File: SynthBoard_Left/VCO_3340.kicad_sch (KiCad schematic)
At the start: 49 parts, among them IC4 AS321KTR-G1, IC5 V3340M, SW1 MFP_240

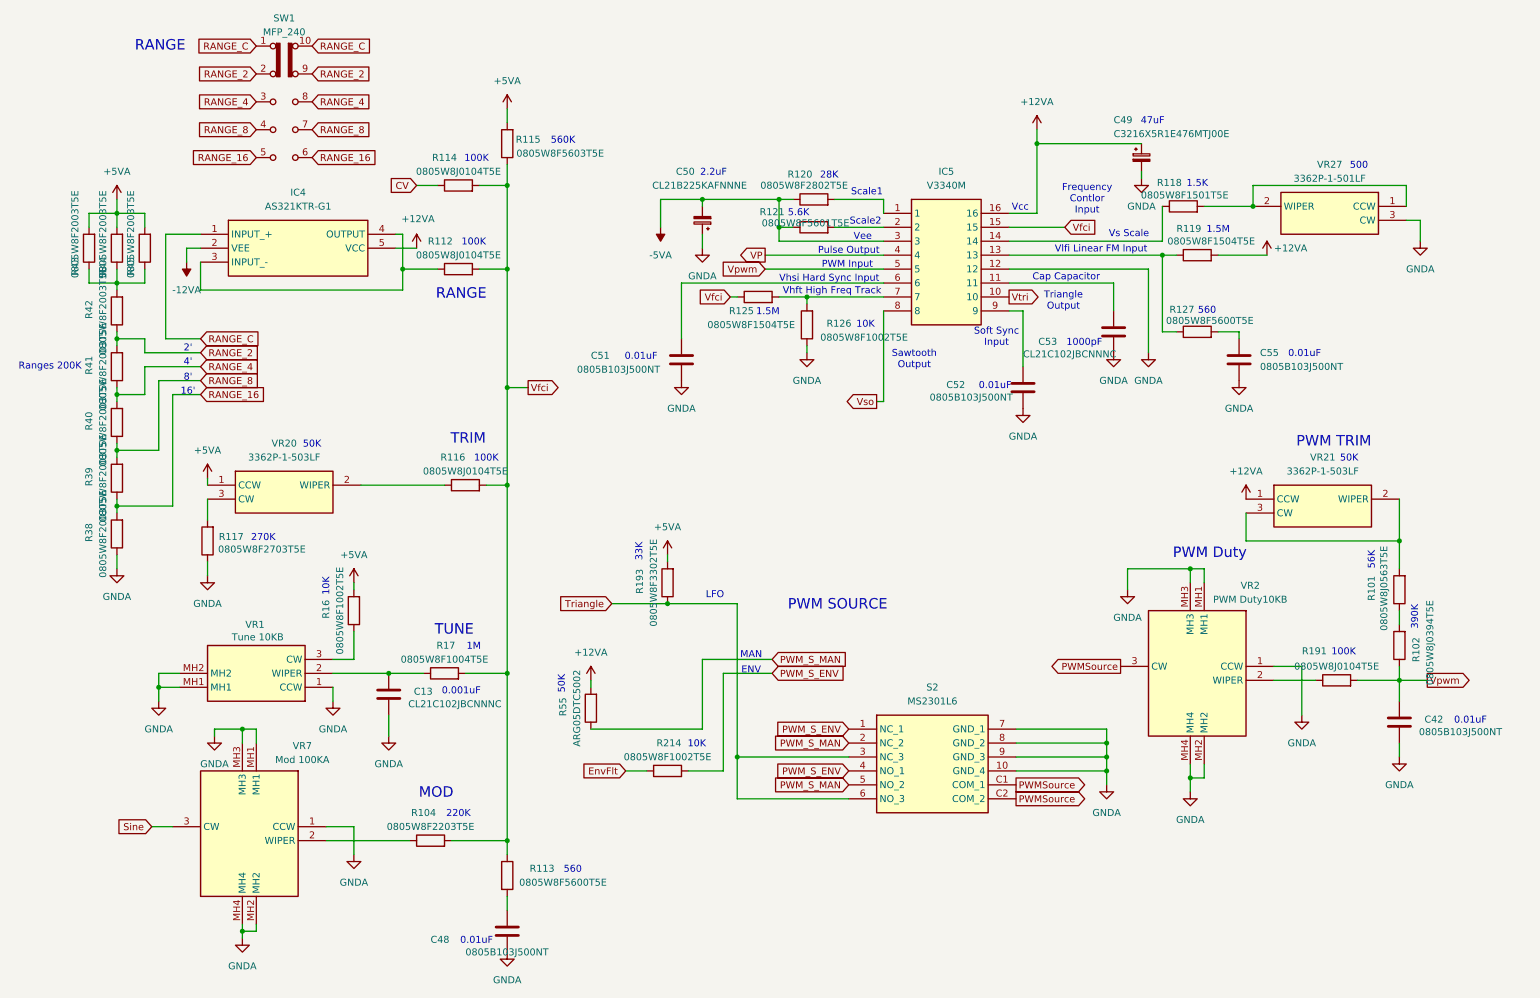
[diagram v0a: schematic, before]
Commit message: SynthBoard_Left
JLCPCBでBasic部品に置き換えた
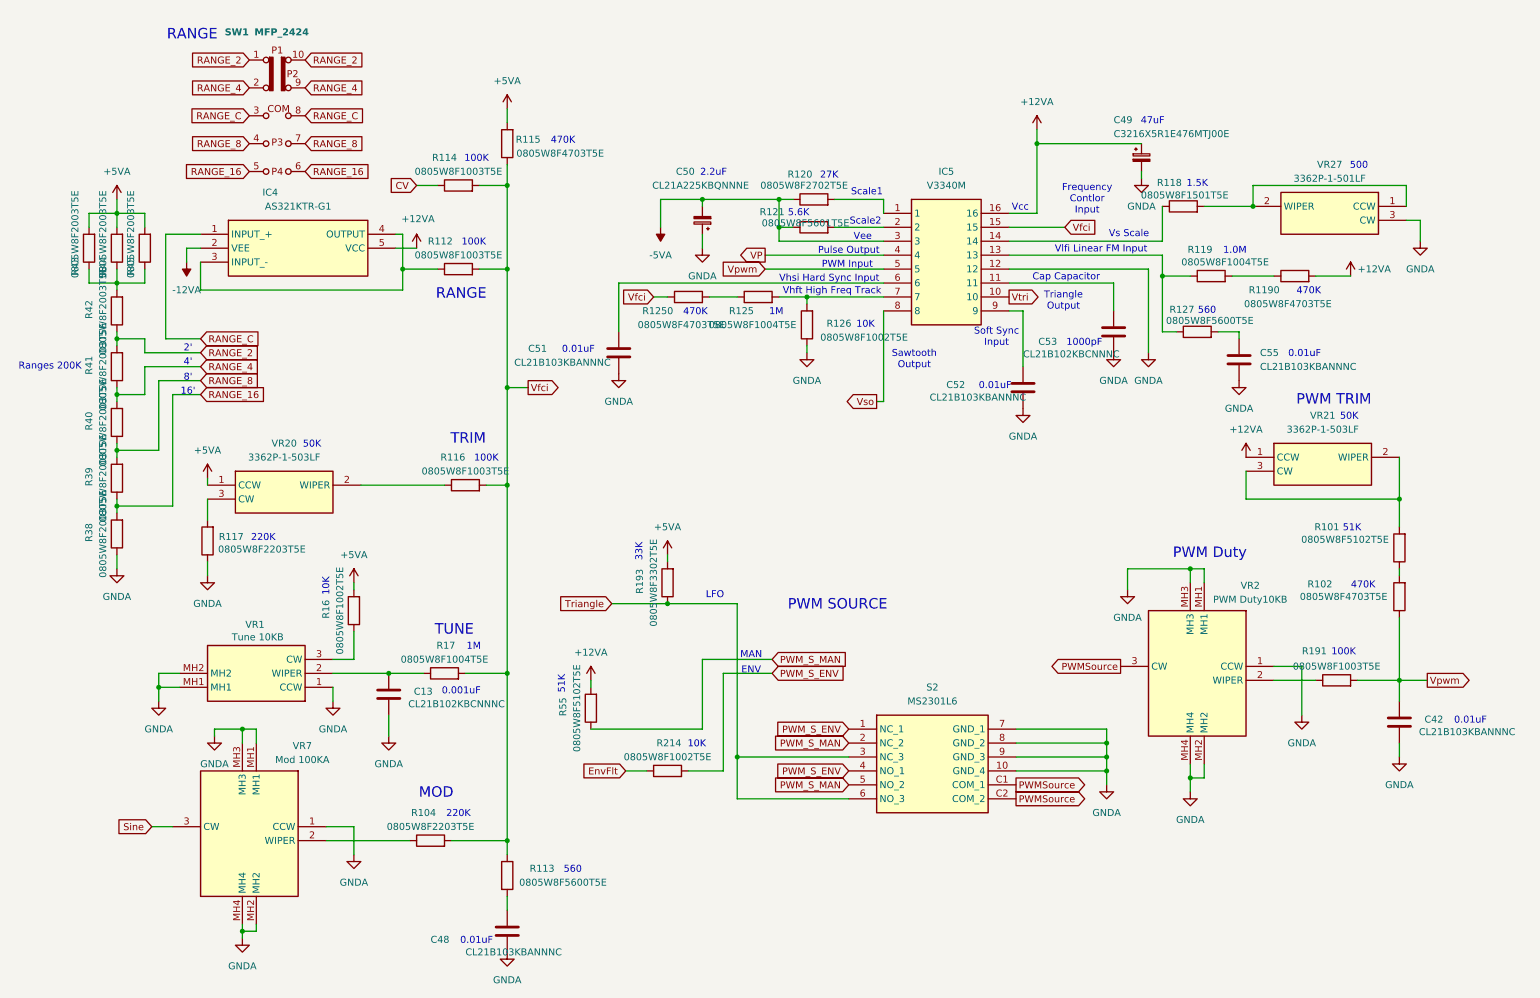
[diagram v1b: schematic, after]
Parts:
- removed SW1: MFP_240, SamacSys_parts:MFP 240, symbol SamacSys_Parts:MFP_240
- added R1190, R1250: 0805W8F4703T5E, Resistor_SMD:R_0805_2012Metric_Pad1.20x1.40mm_HandSolder, symbol Device:R
- added SW1: MFP_2424, SamacSys_parts:MFP 2424, symbol SamacSys_Parts:MFP_2424
- C13: value CL21C102JBCNNNC -> CL21B102KBCNNNC
- C42, C48, C51, C52, C55: value 0805B103J500NT -> CL21B103KBANNNC
- C50: value CL21B225KAFNNNE -> CL21A225KBQNNNE
- C53: value CL21C102JBCNNNC -> CL21B102KBCNNNC; footprint Resistor_SMD:R_0805_2012Metric_Pad1.20x1.40mm_HandSolder -> Capacitor_SMD:C_0805_2012Metric_Pad1.18x1.45mm_HandSolder
- R101: value 0805W8J0563T5E -> 0805W8F5102T5E
- R102: value 0805W8J0394T5E -> 0805W8F4703T5E
- R112, R114, R116, R191: value 0805W8J0104T5E -> 0805W8F1003T5E
- R115: value 0805W8F5603T5E -> 0805W8F4703T5E
- R117: value 0805W8F2703T5E -> 0805W8F2203T5E
- R119, R125: value 0805W8F1504T5E -> 0805W8F1004T5E
- R120: value 0805W8F2802T5E -> 0805W8F2702T5E
- R55: value ARG05DTC5002 -> 0805W8F5102T5E
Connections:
- net +12VA: now also R1190.2; no longer R119.2
- net RANGE_16: now also SW1.5 (E), SW1.6 (F)
- net RANGE_2: now also SW1.1 (A), SW1.10 (J)
- net RANGE_4: now also SW1.2 (B), SW1.9 (I)
- net RANGE_8: now also SW1.4 (D), SW1.7 (G)
- net RANGE_C: now also SW1.3 (C), SW1.8 (H)
- net Vfci: now also R1250.1; no longer R125.1
- new net: R125.1, R1250.2
- new net: R119.2, R1190.1
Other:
- note added: "1.0M"
- note added: "27K"
- note added: "470K"
- note added: "51K"
- note removed: "1.5M"
- note removed: "270K"
- note removed: "28K"
- note removed: "390K"
- note removed: "560K"
- note removed: "56K"
- moved on the sheet: C51, R101, R102, R119, VR21

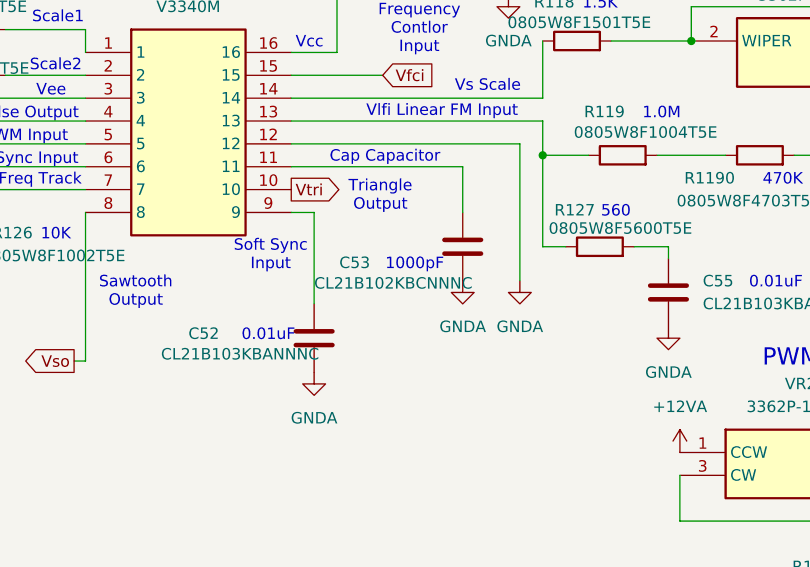
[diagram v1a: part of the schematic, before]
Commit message: MC2
まとめて登録
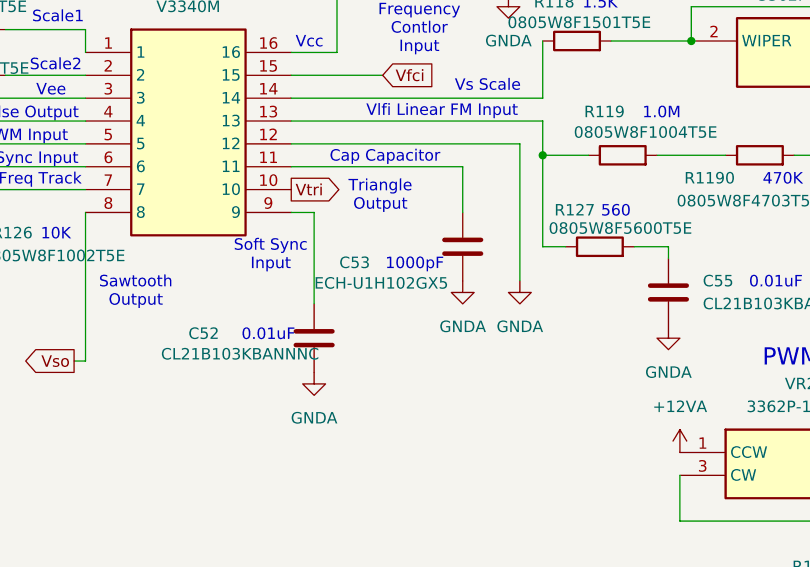
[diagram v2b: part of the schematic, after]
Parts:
- C53: value CL21B102KBCNNNC -> ECH-U1H102GX5
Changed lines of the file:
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@@
 			)
 		)
-		(property "Value" "CL21B102KBCNNNC"
+		(property "Value" "ECH-U1H102GX5"
 			(at 201.93 73.914 0)
 			(effects
